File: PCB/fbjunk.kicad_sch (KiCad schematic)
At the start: 3 parts

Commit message: fix footprint pin 2
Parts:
- C1: footprint 000_LOCAL:FIL_NFM18CC101R1C3D -> 000_LOCAL:FIL_NFM18CC101R1C3D_modified
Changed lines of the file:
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@@
 			)
 		)
-		(property "Footprint" "000_LOCAL:FIL_NFM18CC101R1C3D"
+		(property "Footprint" "000_LOCAL:FIL_NFM18CC101R1C3D_modified"
 			(at 152.4 91.44 90)
 			(effects

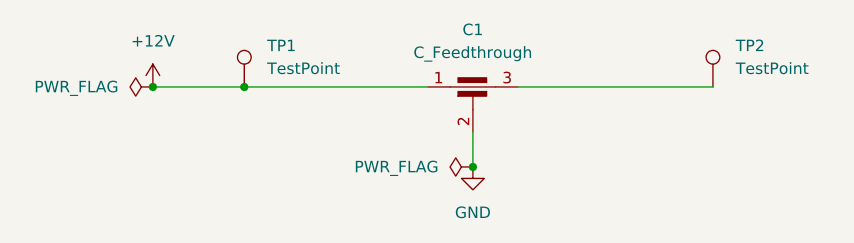
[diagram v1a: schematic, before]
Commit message: add hack inverted pinout symbol
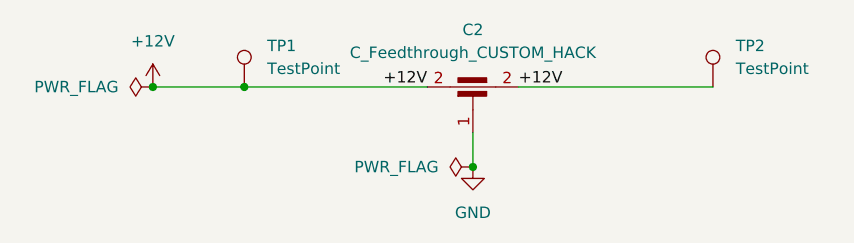
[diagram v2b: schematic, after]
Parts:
- removed C1: C_Feedthrough, 000_LOCAL:FIL_NFM18CC101R1C3D_modified, symbol Device:C_Feedthrough
- added C2: C_Feedthrough_CUSTOM_HACK, 000_LOCAL:C_0603_FeedThrough, symbol 000_LOCAL:C_Feedthrough_CUSTOM_HACK
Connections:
- net +12V: now also TP2.1, C2.2
- net GND: now also C2.1, C2.3
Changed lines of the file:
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@@
+		)
+	)
+	(label "+12V"
+		(at 147.32 88.9 180)
+		(effects
+			(font
+				(size 1.27 1.27)
+			)
+			(justify right bottom)
+		)
+	)
+	(label "+12V"
+		(at 157.48 88.9 0)
+		(effects
+			(font
+				(size 1.27 1.27)
+			)
+			(justify left bottom)
 		)
 	)
@@
 	)
 	(symbol
+		(lib_id "000_LOCAL:C_Feedthrough_CUSTOM_HACK")
+		(at 152.4 91.44 0)
+		(unit 1)
+		(exclude_from_sim no)
+		(in_bom yes)
+		(on_board yes)
+		(dnp no)
+		(fields_autoplaced yes)
+		(property "Reference" "C2"
+			(at 152.4 82.55 0)
+			(effects
+				(font
+					(size 1.27 1.27)
+				)
+			)
+		)
+		(property "Value" "C_Feedthrough_CUSTOM_HACK"
+			(at 152.4 85.09 0)
+			(effects
+				(font
+					(size 1.27 1.27)
+				)
+			)
+		)
+		(property "Footprint" "000_LOCAL:C_0603_FeedThrough"
+			(at 152.4 91.44 90)
+			(effects
+				(font
+					(size 1.27 1.27)
+				)
+				(hide yes)
+			)
+		)
+		(property "Datasheet" "~"
+			(at 152.4 91.44 90)
+			(effects
+				(font
+					(size 1.27 1.27)
+				)
+				(hide yes)
+			)
+		)
+		(property "Description" "Feedthrough capacitor"
+			(at 152.4 91.44 0)
+			(effects
+				(font
+					(size 1.27 1.27)
+				)
+				(hide yes)
+			)
+		)
+		(pin "3"
+		)
+		(pin "2"
+		)
+		(pin "1"
+		)
+		(pin "2"
+		)
+		(instances
+			(project ""
+				(path "/a1729eb5-34ff-42bf-ae94-44c69c5f7c01"
+					(reference "C2")
+					(unit 1)
+				)
+			)
+		)
+	)
+	(symbol
 		(lib_id "Connector:TestPoint")
 		(at 127 88.9 0)
@@
 					(unit 1)
 				)
-			)
-		)
-	)
-	(symbol
-		(lib_id "Device:C_Feedthrough")
-		(at 152.4 91.44 0)
-		(unit 1)
-		(exclude_from_sim no)
-		(in_bom yes)
-		(on_board yes)
-		(dnp no)
-		(fields_autoplaced yes)
-		(property "Reference" "C1"
-			(at 152.4 82.55 0)
-			(effects
-				(font
-					(size 1.27 1.27)
-				)
-			)
-		)
-		(property "Value" "C_Feedthrough"
-			(at 152.4 85.09 0)
-			(effects
-				(font
-					(size 1.27 1.27)
-				)
-			)
-		)
-		(property "Footprint" "000_LOCAL:FIL_NFM18CC101R1C3D_modified"
-			(at 152.4 91.44 90)
-			(effects
-				(font
-					(size 1.27 1.27)
-				)
-				(hide yes)
-			)
-		)
-		(property "Datasheet" "datasheets/NFM18CC101R1C3-01.pdf"
-			(at 152.4 91.44 90)
-			(effects
-				(font
-					(size 1.27 1.27)
-				)
-				(hide yes)
-			)
-		)
-		(property "Description" "Feedthrough capacitor"
-			(at 152.4 91.44 0)
-			(effects
-				(font
-					(size 1.27 1.27)
-				)
-				(hide yes)
-			)
-		)
-		(pin "3"
-		)
-		(pin "2"
-		)
-		(pin "1"
-		)
-		(instances
-			(project ""
-				(path "/a1729eb5-34ff-42bf-ae94-44c69c5f7c01"
-					(reference "C1")
-					(unit 1)
-				)
